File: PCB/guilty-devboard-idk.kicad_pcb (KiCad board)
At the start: 6 copper layers, 17.8 x 21.2 mm, 56 parts, among them J1 USB_C_Receptacle_USB2.0_16P, Q1 SP2038CNQ, U1 nRF54LM20A-QGAA, U2 SGM40567-4.2XG/TR, U3 Xiao nRF52840 Connectors, U5 FH9261-G3JH, U6 BD83070GWL-E2, Y1 32MHz, Y2 32.768kHz

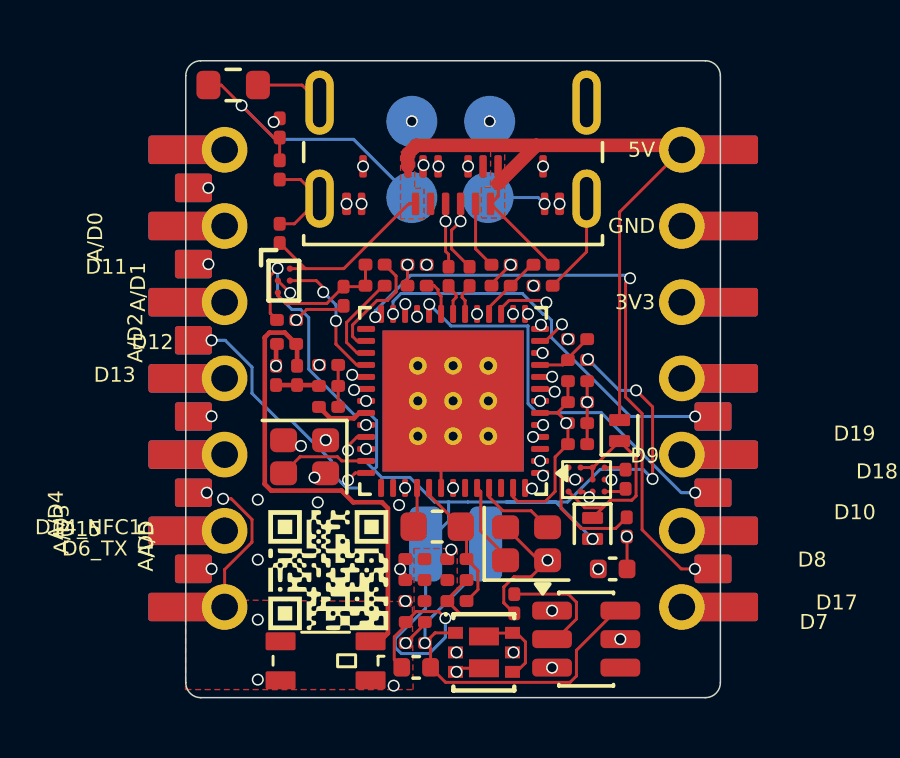
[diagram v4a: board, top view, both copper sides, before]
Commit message: update routing to make antenna better
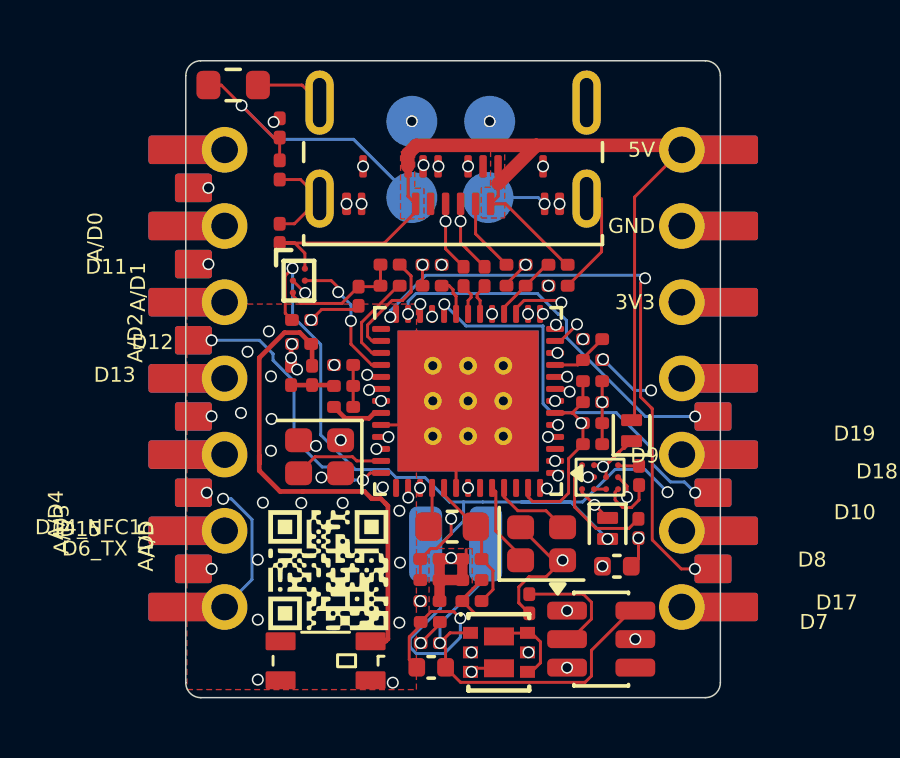
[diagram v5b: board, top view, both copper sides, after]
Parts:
- moved C1 0.50 mm to (88.5, 58.5)
- moved C11 0.50 mm to (85.9, 54.6)
- moved C12 0.50 mm to (83.1, 66.5)
- moved C13 0.50 mm to (87.3, 54.6)
- moved C15 0.50 mm to (78.4, 57.6)
- moved C16 0.50 mm to (83.1, 67.3)
- moved C17 0.50 mm to (78.8, 55.7)
- moved C18 0.50 mm to (80.2, 57.2)
- moved C2 0.50 mm to (88.5, 57.8)
- moved C3 0.50 mm to (78.8, 56.5)
- moved C4 0.50 mm to (84.5, 65.1)
- moved C5 0.50 mm to (83.0, 64.4)
- moved C6 0.50 mm to (84.5, 64.4)
- moved C7 0.50 mm to (83.0, 65.1)
- moved C8 0.50 mm to (88.5, 59.9)
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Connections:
- U1 pad 41: unconnected-(U1C-P1.18-Pad41) -> GND
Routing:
- net /P1.01_NFC1: track 18.7 -> 13.2 mm
- net Net-(U1A-DECA): track 2.45 -> 6.55 mm
- net GND: track 30.2 -> 33.0 mm, vias 30 -> 42
- net VBUS: track 32.0 -> 34.0 mm
- net Net-(D6-K): track 7.24 -> 5.44 mm, vias 0 -> 2
- net /P1.09_D6: track 14.3 -> 16.0 mm
- net /P1.06_A/D3: track 14.8 -> 16.1 mm
- net Net-(U6-LX2): track 0.74 -> 1.90 mm
- net /SWDCLK: track 15.5 -> 14.4 mm
- net /P1.02_NFC2: track 19.3 -> 18.4 mm
- net Net-(U1A-DECRF): track 7.08 -> 6.42 mm
- net Net-(AE1-FEED): track 16.2 -> 16.8 mm
- net /P0.03_GRTC.PWM: track 13.2 -> 12.6 mm
- net /P1.15_D13: track 8.98 -> 9.53 mm
- net /RESET: track 23.0 -> 23.5 mm
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
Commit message: update readme a bit
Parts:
- moved C23 0.40 mm to (89.8, 63.0)
- moved C19 0.28 mm to (89.2, 64.2)
- moved D6 0.27 mm to (88.9, 62.9)
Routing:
- net +BATT: track 41.7 -> 40.0 mm
- net +3V3: track 7.65 -> 9.17 mm, vias 4 -> 5
- net Net-(U6-LX2): track 1.90 -> 0.80 mm
- net GND: track 33.0 -> 32.1 mm
- net /P2.01_SPIM.SCK: track 5.57 -> 6.32 mm
- net Net-(U6-REF): track 4.06 -> 3.89 mm, vias 0 -> 2
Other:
- board size 17.8 x 21.2 mm -> 17.8 x 21 mm

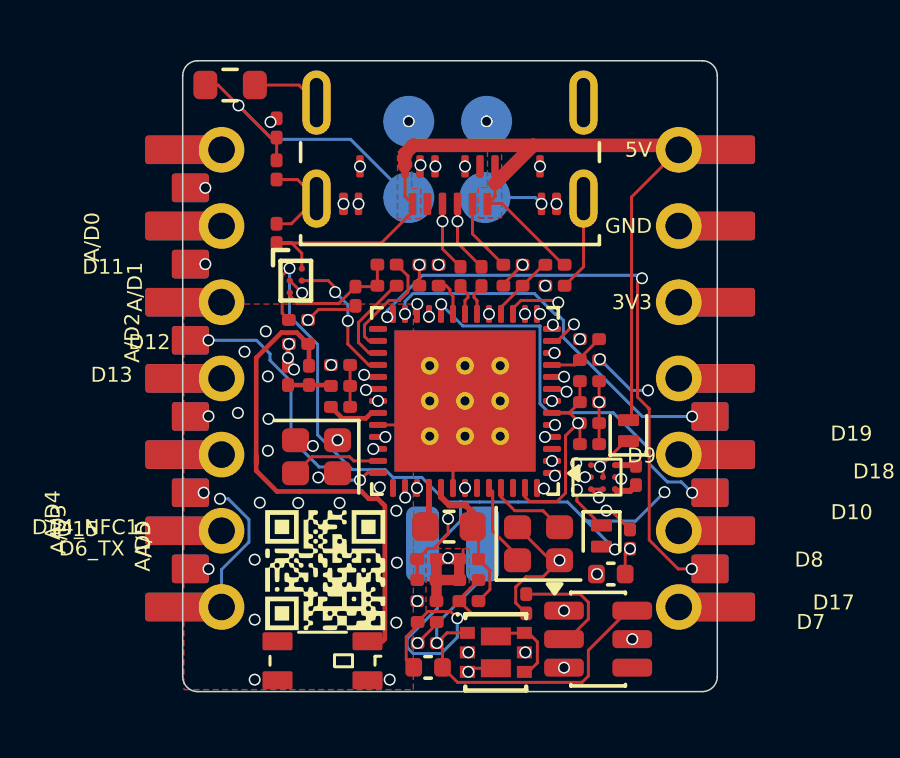
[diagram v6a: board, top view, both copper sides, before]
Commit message: improve via fencing and make it slightly longer for tolerance
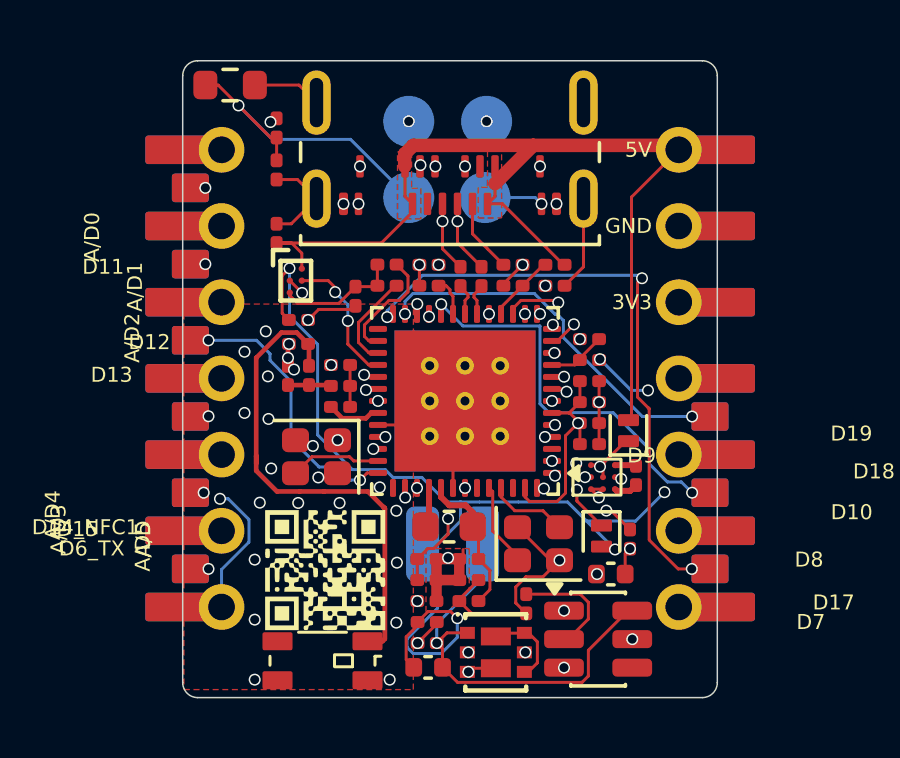
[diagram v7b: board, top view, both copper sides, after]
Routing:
- net /P1.06_A/D3: track 16.1 -> 15.5 mm
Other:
- board size 17.8 x 21 mm -> 17.8 x 21.2 mm
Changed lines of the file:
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@@
 	)
 	(gr_line
-		(start 74.91 67.6)
+		(start 74.91 67.808)
 		(end 74.91 47.58)
 		(stroke
@@
 	)
 	(gr_arc
-		(start 75.41 68.108)
-		(mid 75.056447 67.961553)
-		(end 74.91 67.608)
+		(start 75.41 68.308)
+		(mid 75.056447 68.161553)
+		(end 74.91 67.808)
 		(stroke
 			(width 0.05)
@@
 	)
 	(gr_line
-		(start 92.23 68.108)
-		(end 75.41 68.108)
+		(start 92.23 68.308)
+		(end 75.41 68.308)
 		(stroke
 			(width 0.05)
@@
 	(gr_line
 		(start 92.73 47.58)
-		(end 92.73 67.608)
+		(end 92.73 67.808)
 		(stroke
 			(width 0.05)
@@
 	)
 	(gr_arc
-		(start 92.73 67.608)
-		(mid 92.583553 67.961553)
-		(end 92.23 68.108)
+		(start 92.73 67.808)
+		(mid 92.583553 68.161553)
+		(end 92.23 68.308)
 		(stroke
 			(width 0.05)
@@
 	)
 	(via
-		(at 77.75 60.08)
-		(size 0.4)
-		(drill 0.3)
-		(layers "F.Cu" "B.Cu")
-		(free yes)
-		(net "GND")
-	)
-	(via
 		(at 79.43 60.97)
 		(size 0.4)
@@
 	)
 	(via
+		(at 77.86 60.67)
+		(size 0.4)
+		(drill 0.3)
+		(layers "F.Cu" "B.Cu")
+		(free yes)
+		(net "GND")
+	)
+	(via
 		(at 86.87 51.85)
 		(size 0.4)
@@
 	)
 	(via
-		(at 76.75 58.82)
+		(at 76.97 58.82)
 		(size 0.4)
 		(drill 0.3)
@@
 	)
 	(segment
+		(start 81.596823 61.95175)
+		(end 81.602412 61.95175)
+		(width 0.1565)
+		(layer "F.Cu")
+		(net "Net-(AE1-FEED)")
+	)
+	(segment
 		(start 78.81 61.436772)
 		(end 78.051699 61.436772)
@@
 	)
 	(segment
-		(start 81.565875 61.834125)
-		(end 81.64825 61.9165)
+		(start 81.081845 61.436772)
+		(end 81.596823 61.95175)
 		(width 0.1565)
 		(layer "F.Cu")
@@
 	)
 	(segment
-		(start 81.41 61.67825)
-		(end 81.565875 61.834125)
+		(start 77.36 56.983724)
+		(end 77.36 60.25)
 		(width 0.1565)
 		(layer "F.Cu")
@@
 	)
 	(segment
-		(start 77.36 56.983724)
-		(end 77.36 60.25)
+		(start 81.602412 61.95175)
+		(end 81.64825 61.997588)
 		(width 0.1565)
 		(layer "F.Cu")
@@
 	)
 	(segment
-		(start 81.64825 66.351749)
-		(end 81.569999 66.43)
+		(start 79.62 61.436772)
+		(end 81.081845 61.436772)
 		(width 0.1565)
 		(layer "F.Cu")
@@
 	)
 	(segment
-		(start 81.64825 61.9165)
-		(end 81.64825 66.351749)
+		(start 81.64825 66.351749)
+		(end 81.569999 66.43)
 		(width 0.1565)
 		(layer "F.Cu")
@@
 	)
 	(segment
-		(start 80.866772 61.436772)
-		(end 81.10825 61.67825)
+		(start 81.64825 61.997588)
+		(end 81.64825 66.351749)
 		(width 0.1565)
 		(layer "F.Cu")
@@
 	)
 	(segment
-		(start 78.81 61.436772)
-		(end 80.866772 61.436772)
+		(start 81.64825 61.997588)
+		(end 81.64825 62.05)
 		(width 0.1565)
 		(layer "F.Cu")
@@
 	)
 	(segment
-		(start 81.10825 61.67825)
-		(end 81.41 61.67825)
+		(start 78.81 61.436772)
+		(end 79.62 61.436772)
 		(width 0.1565)
 		(layer "F.Cu")
@@
 	)
 	(segment
-		(start 75.365 47.545)
-		(end 75.35 47.53)
-		(width 0.1)
-		(layer "F.Cu")
-		(net "/RESET")
-	)
-	(segment
 		(start 78.04 49.64)
 		(end 77.840001 49.64)
@@
 	)
 	(segment
-		(start 85.9331 57.691875)
-		(end 81.594753 57.691875)
-		(width 0.1)
-		(layer "In2.Cu")
-		(net "/P1.06_A{slash}D3")
-	)
-	(segment
-		(start 87.6 56.024975)
-		(end 85.9331 57.691875)
+		(start 80.450304 57.199696)
+		(end 81.102574 57.199696)
 		(width 0.1)
 		(layer "In2.Cu")
@@
 	)
 	(segment
-		(start 87.429977 55.140023)
-		(end 87.6 55.310046)
+		(start 76.48675 57.95)
+		(end 79.7 57.95)
 		(width 0.1)
 		(layer "In2.Cu")
@@
 	)
 	(segment
-		(start 81.102574 57.199696)
-		(end 80.450304 57.199696)
+		(start 76.205 57.66825)
+		(end 76.48675 57.95)
 		(width 0.1)
 		(layer "In2.Cu")
@@
 	)
 	(segment
-		(start 76.205 57.66825)
-		(end 77.203625 58.666875)
+		(start 87.6 56.024975)
+		(end 87.6 55.310046)
 		(width 0.1)
 		(layer "In2.Cu")
@@
 	)
 	(segment
-		(start 87.6 55.310046)
+		(start 85.9331 57.691875)
 		(end 87.6 56.024975)
 		(width 0.1)
@@
 	)
 	(segment
-		(start 80.450304 57.199696)
-		(end 79.98175 57.66825)
+		(start 79.7 57.95)
+		(end 80.450304 57.199696)
 		(width 0.1)
 		(layer "In2.Cu")
@@
 	)
 	(segment
-		(start 78.983125 58.666875)
-		(end 79.98175 57.66825)
+		(start 87.6 55.310046)
+		(end 87.429977 55.140023)
 		(width 0.1)
 		(layer "In2.Cu")
@@
 	)
 	(segment
-		(start 77.203625 58.666875)
-		(end 78.983125 58.666875)
+		(start 81.594753 57.691875)
+		(end 85.9331 57.691875)
 		(width 0.1)
 		(layer "In2.Cu")
@@
 	)
 	(segment
-		(start 81.594753 57.691875)
-		(end 81.102574 57.199696)
+		(start 81.102574 57.199696)
+		(end 81.594753 57.691875)
 		(width 0.1)
 		(layer "In2.Cu")
@@
 	)
 	(segment
-		(start 82.729186 56.040814)
-		(end 82.729186 55.189402)
+		(start 76.547383 61.681958)
+		(end 77.117 61.11234)
 		(width 0.1)
 		(layer "In4.Cu")
@@
 	)
 	(segment
-		(start 81.794161 56.040814)
-		(end 82.729186 56.040814)
+		(start 82.729186 56.040814)
+		(end 82.729186 55.189402)
 		(width 0.1)
 		(layer "In4.Cu")
@@
 	)
 	(segment
-		(start 77.37 60.859341)
-		(end 77.37 58.57)
+		(start 77.117 60.14)
+		(end 77.37 59.887)
 		(width 0.1)
 		(layer "In4.Cu")
@@
 	)
 	(segment
-		(start 76.547383 61.681958)
-		(end 77.37 60.859341)
+		(start 77.117 61.11234)
+		(end 77.117 60.14)
 		(width 0.1)
 		(layer "In4.Cu")
@@
 		(net "/P1.09_D6")
 	)
+	(segment
+		(start 77.37 59.887)
+		(end 77.37 58.57)
+		(width 0.1)
+		(layer "In4.Cu")
+		(net "/P1.09_D6")
+	)
+	(segment
+		(start 81.794161 56.040814)
+		(end 82.729186 56.040814)
+		(width 0.1)
+		(layer "In4.Cu")
+		(net "/P1.09_D6")
+	)
 	(via
 		(at 87.22 60.42)
@@
 	)
 	(segment
-		(start 76.01975 61.32025)
-		(end 77.165604 61.32025)
+		(start 75.86175 61.47825)
+		(end 76.01975 61.32025)
 		(width 0.1)
 		(layer "In2.Cu")
@@
 	)
 	(segment
-		(start 75.86175 61.47825)
-		(end 76.01975 61.32025)
+		(start 76.01975 61.32025)
+		(end 78.45975 61.32025)
 		(width 0.1)
 		(layer "In2.Cu")
@@
 	)
 	(segment
-		(start 87.95 55.964925)
-		(end 87.95 55.865768)
+		(start 78.45975 61.32025)
+		(end 79.16 60.62)
 		(width 0.1)
 		(layer "In2.Cu")
@@
 	)
 	(segment
-		(start 86.314368 60.786013)
-		(end 87.67 59.43038)
+		(start 87.95 55.964925)
+		(end 87.95 55.865768)
 		(width 0.1)
 		(layer "In2.Cu")
@@
 	)
 	(segment
-		(start 77.165604 61.32025)
-		(end 77.865854 60.62)
+		(start 86.314368 60.786013)
+		(end 87.67 59.43038)
 		(width 0.1)
 		(layer "In2.Cu")
@@
 	)
 	(segment
-		(start 77.865854 60.62)
+		(start 79.16 60.62)
 		(end 81.473987 60.62)
 		(width 0.1)

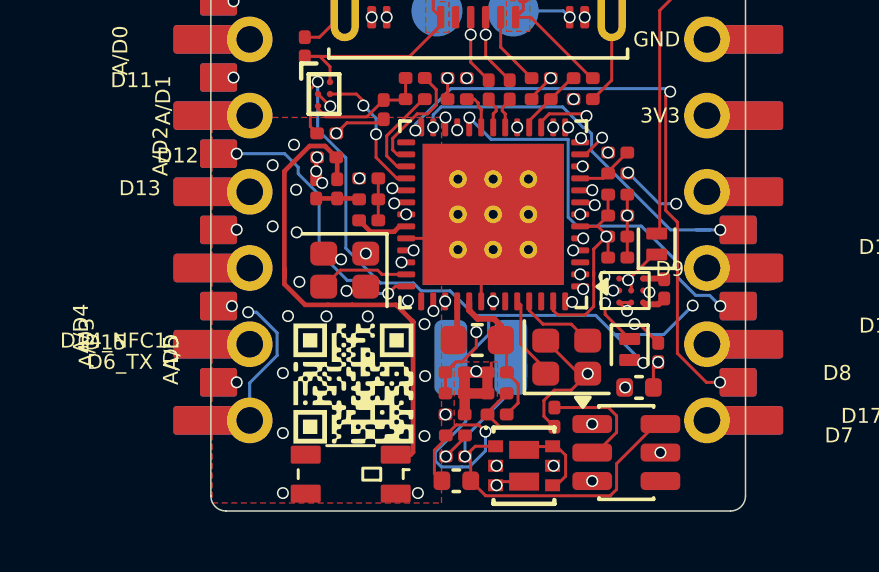
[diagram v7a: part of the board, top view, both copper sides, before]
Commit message: misc notes and whatnot on schematic, got rid of unnecessary via/GNDed pin
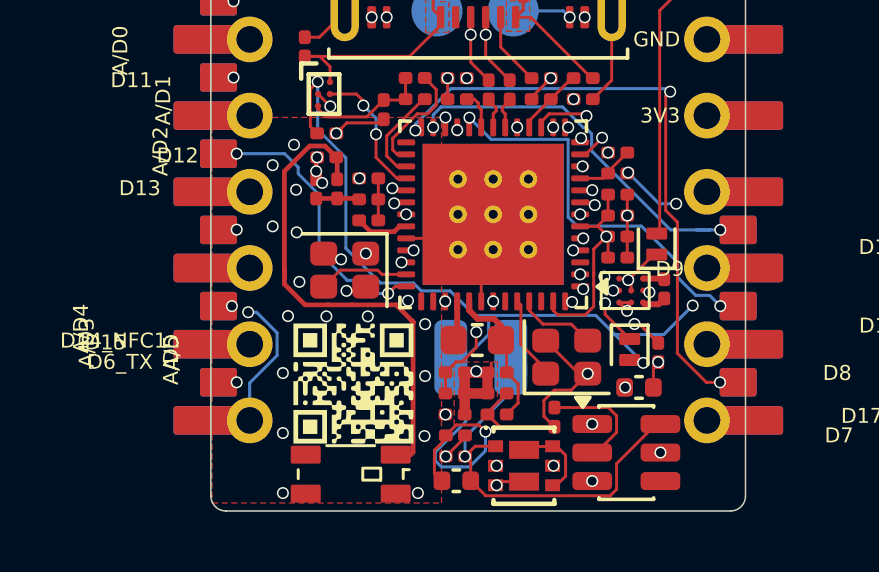
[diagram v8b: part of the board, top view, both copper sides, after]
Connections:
- U1 pad 41: GND -> unconnected-(U1C-P1.18-Pad41)
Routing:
- net GND: track 32.1 -> 31.8 mm, vias 42 -> 41
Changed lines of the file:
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@@
 			(layers "F.Cu" "F.Mask" "F.Paste")
 			(roundrect_rratio 0.25)
-			(net "GND")
+			(net "unconnected-(U1C-P1.18-Pad41)")
 			(pinfunction "P1.18_41")
 			(pintype "bidirectional")
@@
 	)
 	(segment
-		(start 82.32 61.633327)
-		(end 82.327164 61.640491)
-		(width 0.1)
-		(layer "F.Cu")
-		(net "GND")
-	)
-	(segment
 		(start 77.315 47.89)
 		(end 78.785 47.89)
-		(width 0.1)
-		(layer "F.Cu")
-		(net "GND")
-	)
-	(segment
-		(start 82.32 61.32)
-		(end 82.32 61.633327)
 		(width 0.1)
 		(layer "F.Cu")
@@
 	)
 	(via
-		(at 82.327164 61.640491)
-		(size 0.4)
-		(drill 0.3)
-		(layers "F.Cu" "B.Cu")
-		(net "GND")
-	)
-	(via
 		(at 79.25 59.92)
 		(size 0.4)
@@
 	)
 	(via
-		(at 82.03 62.08)
-		(size 0.4)
-		(drill 0.3)
+		(at 82.05 62.08)
+		(size 0.4)
+		(drill 0.3)
